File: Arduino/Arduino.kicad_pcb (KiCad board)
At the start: 2 copper layers, 13 parts, among them J5 ICSP, J6 Digital, U1 ATmega328P-P, U2 AMS1117-5.0, Y1 16MHz

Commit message: Some changes in arduino board.
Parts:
- added C13: 22pF, Capacitor_SMD:C_0805_2012Metric, F.Cu at (151.4, 31.5)
- added C14: 22pF, Capacitor_SMD:C_0805_2012Metric, F.Cu at (151.4, 29.3)
- added C15: 100nF, Capacitor_SMD:C_0805_2012Metric, F.Cu at (135.7, 32.9)
- added C16: 100nF, Capacitor_SMD:C_0805_2012Metric, F.Cu at (135.7, 30.8)
- added D10: 1N4148WT, Diode_SMD:D_SOD-523, F.Cu at (217.5, 75.0)
- added D11: LED, LED_SMD:LED_0805_2012Metric, F.Cu at (196.6, 82.0)
- added D12: 1N4148WT, Diode_SMD:D_SOD-523, F.Cu at (195.2, 75.5)
- added D3: LED_TX, Diode_SMD:D_0805_2012Metric, F.Cu at (146.1, 39.7)
- added D4: LED_RX, Diode_SMD:D_0805_2012Metric, F.Cu at (136.0, 39.7)
- added D5: LED, LED_SMD:LED_0805_2012Metric, F.Cu at (174.8, 82.6)
- added D6: 1N4148WT, Diode_SMD:D_SOD-523, F.Cu at (173.5, 76.1)
- added D7: LED, LED_SMD:LED_0805_2012Metric, F.Cu at (240.5, 81.8)
- added D8: 1N4148WT, Diode_SMD:D_SOD-523, F.Cu at (239.2, 75.3)
- added D9: LED, LED_SMD:LED_0805_2012Metric, F.Cu at (218.8, 81.5)
- added J1: Barrel_Jack_Switch, Connector_BarrelJack:BarrelJack_Wuerth_6941xx301002, F.Cu at (52.8, 28.0)
- added J11: USB_C_Receptacle_USB2.0, Connector_USB:USB_C_Receptacle_G-Switch_GT-USB-7010ASV, F.Cu at (142.9, 57.9)
- added J12: USB_B, Connector_USB:USB_B_OST_USB-B1HSxx_Horizontal, F.Cu at (144.3, 48.4)
- added J13: Conn_01x04, Connector_PinHeader_2.54mm:PinHeader_1x04_P2.54mm_Vertical, F.Cu at (147.0, 27.9)
- added J14: Screw_Terminal_01x12, TerminalBlock_RND:TerminalBlock_RND_205-00297_1x12_P5.08mm_Horizontal, F.Cu at (178.0, 99.4)
- added J15: Conn_01x01, Connector_PinHeader_2.54mm:PinHeader_1x01_P2.54mm_Vertical, F.Cu at (181.8, 85.8)
- added J16: Conn_01x01, Connector_PinHeader_2.54mm:PinHeader_1x01_P2.54mm_Vertical, F.Cu at (247.5, 85.0)
- added J17: Conn_01x01, Connector_PinHeader_2.54mm:PinHeader_1x01_P2.54mm_Vertical, F.Cu at (225.8, 84.7)
- added J18: Conn_01x01, Connector_PinHeader_2.54mm:PinHeader_1x01_P2.54mm_Vertical, F.Cu at (203.5, 85.2)
- added J2: Vcc, TerminalBlock_Phoenix:TerminalBlock_Phoenix_MKDS-1,5-2-5.08_1x02_P5.08mm_Horizontal, F.Cu at (63.1, 32.3)
- added J3: Conn_01x03, Connector_PinHeader_2.54mm:PinHeader_1x03_P2.54mm_Vertical, F.Cu at (61.8, 40.5)
- added JP1: Vusb, Jumper:SolderJumper-2_P1.3mm_Bridged2Bar_RoundedPad1.0x1.5mm, B.Cu at (149.0, 48.2)
- added JP2: SolderJumper_3_Bridged12, Jumper:SolderJumper-3_P1.3mm_Bridged12_RoundedPad1.0x1.5mm, F.Cu at (177.3, 107.8)
- added JP3: ~, Jumper:SolderJumper-2_P1.3mm_Bridged_RoundedPad1.0x1.5mm, F.Cu at (181.9, 82.2)
- added JP4: ~, Jumper:SolderJumper-2_P1.3mm_Bridged_RoundedPad1.0x1.5mm, F.Cu at (247.6, 81.4)
- added JP5: ~, Jumper:SolderJumper-2_P1.3mm_Bridged_RoundedPad1.0x1.5mm, F.Cu at (225.9, 81.1)
- added JP6: ~, Jumper:SolderJumper-2_P1.3mm_Bridged_RoundedPad1.0x1.5mm, F.Cu at (203.7, 81.6)
- added K1: G5LE-1, Relay_THT:Relay_SPDT_Omron-G5LE-1, F.Cu at (175.8, 69.9)
- added K2: G5LE-1, Relay_THT:Relay_SPDT_Omron-G5LE-1, F.Cu at (241.6, 69.1)
- added K3: G5LE-1, Relay_THT:Relay_SPDT_Omron-G5LE-1, F.Cu at (219.8, 68.8)
- added K4: G5LE-1, Relay_THT:Relay_SPDT_Omron-G5LE-1, F.Cu at (197.6, 69.3)
- added Q3: SS8050, Package_TO_SOT_SMD:SOT-23, F.Cu at (178.5, 76.5)
- added Q4: SS8050, Package_TO_SOT_SMD:SOT-23, F.Cu at (244.2, 75.7)
- added Q5: SS8050, Package_TO_SOT_SMD:SOT-23, F.Cu at (222.5, 75.4)
- added Q6: SS8050, Package_TO_SOT_SMD:SOT-23, F.Cu at (200.2, 75.9)
- added R10: 1k, Resistor_SMD:R_0805_2012Metric, F.Cu at (142.0, 39.7)
- added R11: 1k, Resistor_SMD:R_0805_2012Metric, F.Cu at (140.0, 39.7)
- added R12: 1k, Resistor_SMD:R_0805_2012Metric, F.Cu at (144.0, 39.7)
- added R13: 1k, Resistor_SMD:R_0805_2012Metric, F.Cu at (172.7, 82.6)
- added R14: 10k, Resistor_SMD:R_0805_2012Metric, F.Cu at (178.9, 82.6)
- added R15: 10k, Resistor_SMD:R_0805_2012Metric, F.Cu at (176.9, 82.6)
- added R16: 1k, Resistor_SMD:R_0805_2012Metric, F.Cu at (238.4, 81.8)
- added R17: 10k, Resistor_SMD:R_0805_2012Metric, F.Cu at (242.6, 81.8)
- added R18: 10k, Resistor_SMD:R_0805_2012Metric, F.Cu at (244.6, 81.8)
- added R19: 10k, Resistor_SMD:R_0805_2012Metric, F.Cu at (220.9, 81.6)
- added R20: 1k, Resistor_SMD:R_0805_2012Metric, F.Cu at (216.7, 81.6)
- added R21: 10k, Resistor_SMD:R_0805_2012Metric, F.Cu at (222.9, 81.6)
- added R22: 10k, Resistor_SMD:R_0805_2012Metric, F.Cu at (198.6, 82.1)
- added R23: 1k, Resistor_SMD:R_0805_2012Metric, F.Cu at (194.5, 82.1)
- added R24: 10k, Resistor_SMD:R_0805_2012Metric, F.Cu at (200.6, 82.1)
- added R5: 5k1, Resistor_SMD:R_0805_2012Metric, F.Cu at (152.5, 48.1)
- added R6: 5k1, Resistor_SMD:R_0805_2012Metric, F.Cu at (133.6, 48.1)
- added R7: 51, Resistor_SMD:R_0805_2012Metric, F.Cu at (148.2, 39.7)
- added R8: 51, Resistor_SMD:R_0805_2012Metric, F.Cu at (150.2, 39.7)
- added R9: 1k, Resistor_SMD:R_0805_2012Metric, F.Cu at (138.0, 39.7)
- added U3: CH340G, Package_SO:SOIC-16_3.9x9.9mm_P1.27mm, F.Cu at (143.2, 33.6)
- added Y2: 12Mhz, Crystal:Crystal_SMD_Abracon_ABM8G-4Pin_3.2x2.5mm, F.Cu at (151.3, 35.5)
- renumbered C9 to C10, C10 to C11, C11 to C12, C7 to C8, C8 to C9, J5 to J8, J6 to J9, R3 to R4
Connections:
- net /Regulador/12V renamed +12V
- net /Regulador/5V renamed /Regulador de Tensao/5V
- C10 pad 2: /Regulador/GND -> GND
- C11 pad 2: /Regulador/GND -> GND
- C12 pad 2: /Regulador/GND -> GND
- C8 pad 2: /Regulador/GND -> GND
- C9 pad 2: /Regulador/GND -> GND
- D1 pad 2: /Regulador/Vin -> /Regulador de Tensao/Vin
- D2 pad 1: /Regulador/GND -> GND
- U2 pad 1: /Regulador/GND -> GND
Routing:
- net GND: track 0.00 -> 133.5 mm, vias 0 -> 6
- net Net-(D1001-K): track 0.00 -> 84.2 mm
- net /12V: track 0.00 -> 60.5 mm
- net /Regulador/GND: track 33.8 -> 0.00 mm, vias 3 -> 0
- net Net-(J12-VBUS): track 0.00 -> 24.5 mm, vias 0 -> 1
- net /Vcc: track 0.00 -> 24.3 mm
- net /GND: track 0.00 -> 23.9 mm, vias 0 -> 8
- net Net-(J12-D+): track 0.00 -> 22.6 mm, vias 0 -> 1
- net Net-(J12-D-): track 0.00 -> 21.0 mm
- net Net-(Q1001-B): track 0.00 -> 20.8 mm
- net Net-(JP1001-B): track 0.00 -> 20.8 mm
- net /INPUT: track 0.00 -> 20.8 mm
- net Net-(U3-XO): track 0.00 -> 19.2 mm
- net Net-(U3-XI): track 0.00 -> 11.9 mm
- net Net-(J11-CC1): track 0.00 -> 11.6 mm
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
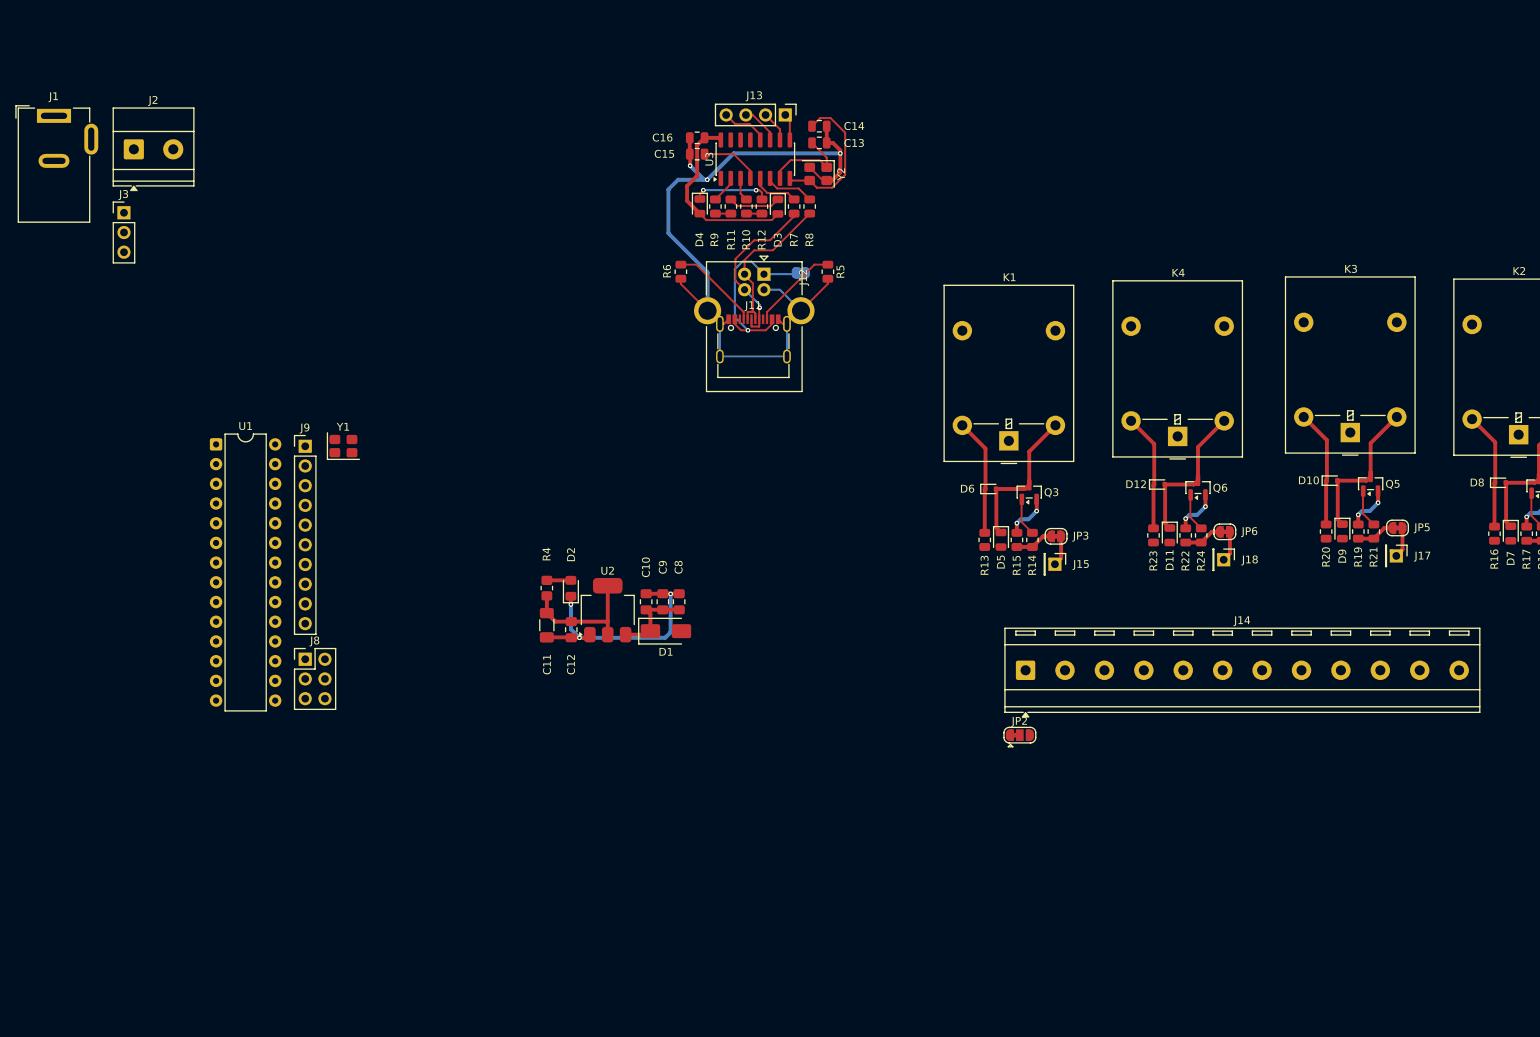
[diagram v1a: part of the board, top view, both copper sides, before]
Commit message: Completed circuit.
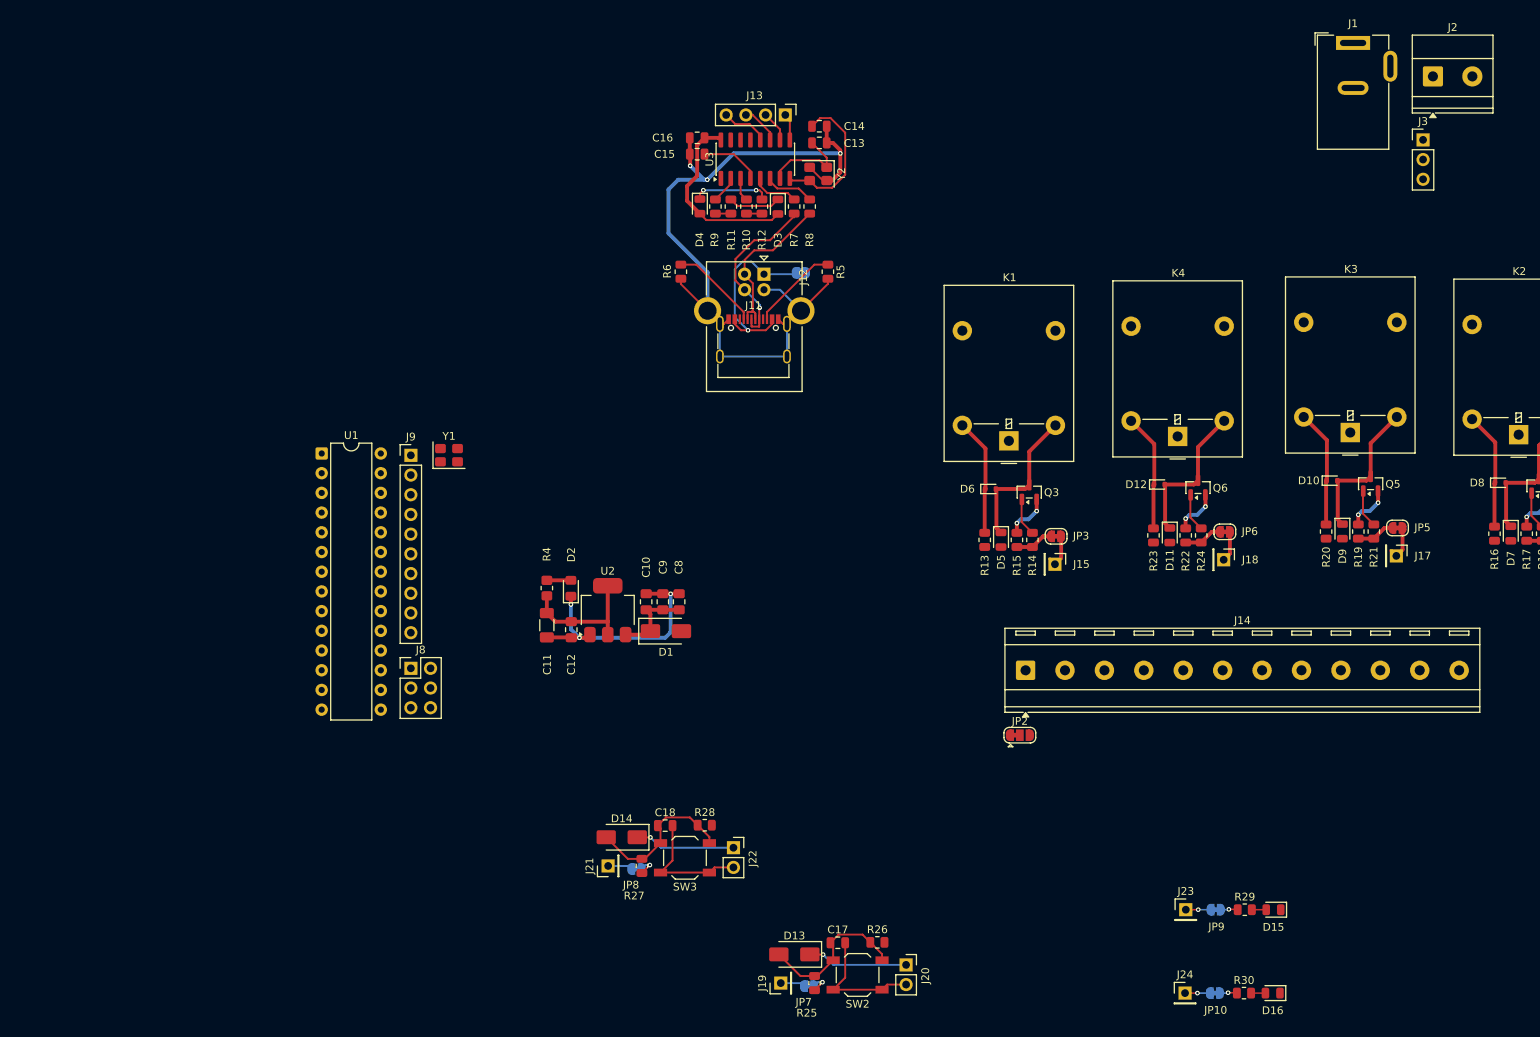
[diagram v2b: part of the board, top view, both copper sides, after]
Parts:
- added C17: 100n, Capacitor_SMD:C_0805_2012Metric, F.Cu at (153.8, 134.6)
- added C18: 100n, Capacitor_SMD:C_0805_2012Metric, F.Cu at (131.6, 119.5)
- added D13: 1N4007, Diode_SMD:D_SMA, F.Cu at (148.2, 136.1)
- added D14: 1N4007, Diode_SMD:D_SMA, F.Cu at (126.0, 121.0)
- added D15: LED, LED_SMD:LED_0805_2012Metric, F.Cu at (209.9, 130.3)
- added D16: LED, LED_SMD:LED_0805_2012Metric, F.Cu at (209.8, 141.1)
- added J19: Pin, Connector_PinHeader_2.54mm:PinHeader_1x01_P2.54mm_Vertical, F.Cu at (146.4, 139.8)
- added J20: Bt_ext, Connector_PinSocket_2.54mm:PinSocket_1x02_P2.54mm_Vertical, F.Cu at (162.6, 137.4)
- added J21: Pin, Connector_PinHeader_2.54mm:PinHeader_1x01_P2.54mm_Vertical, F.Cu at (124.2, 124.7)
- added J22: Bt_ext, Connector_PinSocket_2.54mm:PinSocket_1x02_P2.54mm_Vertical, F.Cu at (140.3, 122.3)
- added J23: Pin, Connector_PinHeader_2.54mm:PinHeader_1x01_P2.54mm_Vertical, F.Cu at (198.7, 130.3)
- added J24: Pin, Connector_PinHeader_2.54mm:PinHeader_1x01_P2.54mm_Vertical, F.Cu at (198.6, 141.1)
- added JP10: A, Jumper:SolderJumper-2_P1.3mm_Bridged_RoundedPad1.0x1.5mm, B.Cu at (202.4, 141.1)
- added JP7: A, Jumper:SolderJumper-2_P1.3mm_Bridged_RoundedPad1.0x1.5mm, B.Cu at (150.1, 140.2)
- added JP8: A, Jumper:SolderJumper-2_P1.3mm_Bridged_RoundedPad1.0x1.5mm, B.Cu at (127.8, 125.1)
- added JP9: A, Jumper:SolderJumper-2_P1.3mm_Bridged_RoundedPad1.0x1.5mm, B.Cu at (202.5, 130.3)
- added R25: 1k, Resistor_SMD:R_0805_2012Metric, F.Cu at (150.8, 139.8)
- added R26: 100k, Resistor_SMD:R_0805_2012Metric, F.Cu at (158.9, 134.5)
- added R27: 1k, Resistor_SMD:R_0805_2012Metric, F.Cu at (128.6, 124.7)
- added R28: 100k, Resistor_SMD:R_0805_2012Metric, F.Cu at (136.7, 119.4)
- added R29: 1k, Resistor_SMD:R_0805_2012Metric, F.Cu at (206.2, 130.3)
- added R30: 1k, Resistor_SMD:R_0805_2012Metric, F.Cu at (206.2, 141.1)
- added SW2: Button, Button_Switch_SMD:SW_SPST_TL3342, F.Cu at (156.3, 138.7)
- added SW3: Button, Button_Switch_SMD:SW_SPST_TL3342, F.Cu at (134.1, 123.6)
- moved J1 167.7 mm to (220.2, 18.6)
- moved J2 167.7 mm to (230.5, 22.9)
- moved J3 167.7 mm to (229.2, 31.1)
- moved J8 13.7 mm to (98.8, 99.2)
- moved J9 13.7 mm to (98.8, 71.7)
- moved U1 13.7 mm to (87.3, 71.5)
- moved Y1 13.7 mm to (103.7, 71.7)
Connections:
- JP2 pad 1: /Reles/5V -> +5V
- JP2 pad 3: /Reles/12V -> +12V
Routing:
- net Net-(D1001-A): track 0.00 -> 44.5 mm
- net /GND: track 23.9 -> 56.6 mm
- net Net-(D1001-K): track 84.2 -> 110.2 mm, vias 0 -> 2
- net Net-(JP1001-B): track 20.8 -> 30.8 mm, vias 0 -> 4
- net /IN: track 0.00 -> 6.40 mm, vias 0 -> 2
- net /OUT: track 0.00 -> 6.33 mm
